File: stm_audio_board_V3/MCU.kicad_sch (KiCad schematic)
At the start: 44 parts, among them P1 USB_C_Plug_USB2.0, SW1 SW_SPST, U1 IS42S16100H-7TL, U16 USBLC6-2P6, U17 W25Q128JVS, U19 FE1.1s, U7 STM32H723ZGTx, Y2 X1E0000210132, Y3 Crystal_GND24

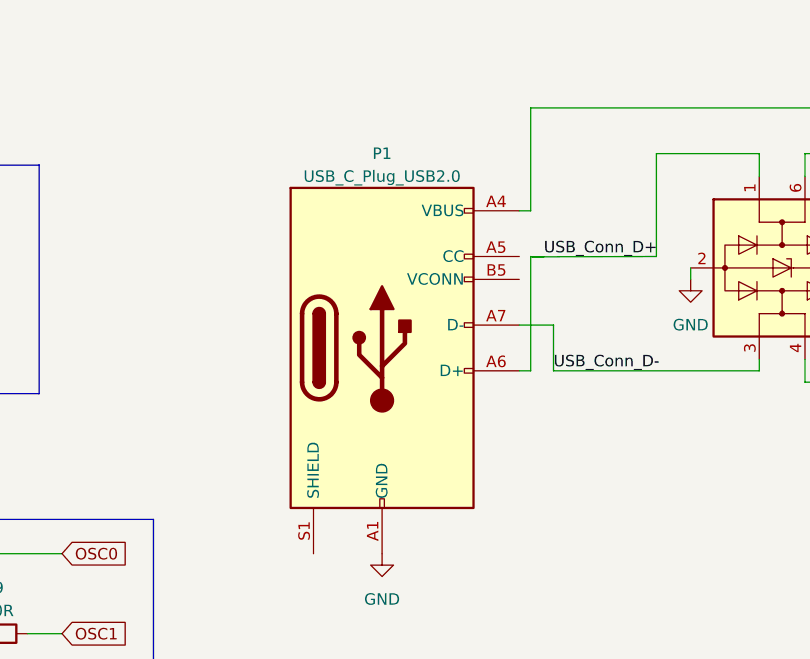
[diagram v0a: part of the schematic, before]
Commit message: Via size increased for economical reasons
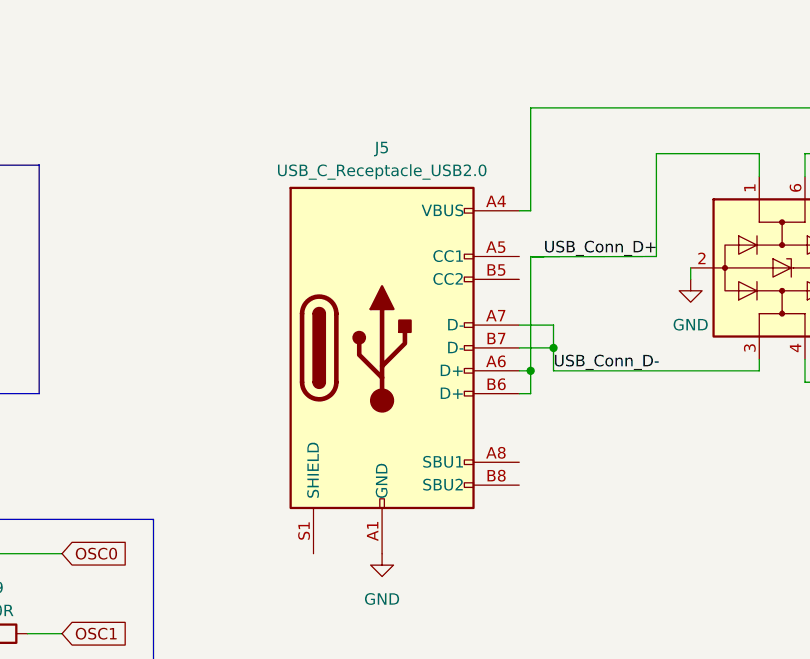
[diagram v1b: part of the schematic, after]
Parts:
- removed P1: USB_C_Plug_USB2.0, Connector_USB:USB_C_Receptacle_XKB_U262-16XN-4BVC11, symbol Connector:USB_C_Plug_USB2.0
- added J5: USB_C_Receptacle_USB2.0, Connector_USB:USB_C_Receptacle_XKB_U262-16XN-4BVC11, symbol Connector:USB_C_Receptacle_USB2.0
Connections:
- net GND: now also J5.A1 (GND), J5.A12 (GND), J5.B1 (GND), J5.B12 (GND)
- net USB_Conn_D+: now also J5.A6 (D+), J5.B6 (D+)
- net USB_Conn_D-: now also J5.A7 (D-), J5.B7 (D-)
- net at C12.1, U19.18 (VBUSM): now also J5.A4 (VBUS), J5.A9 (VBUS), J5.B4 (VBUS), J5.B9 (VBUS)
